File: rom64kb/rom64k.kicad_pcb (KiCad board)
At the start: 2 copper layers, 81.3 x 65.3 mm, 3 parts, among them P1 CONN_02X25, U2 SST39SF010

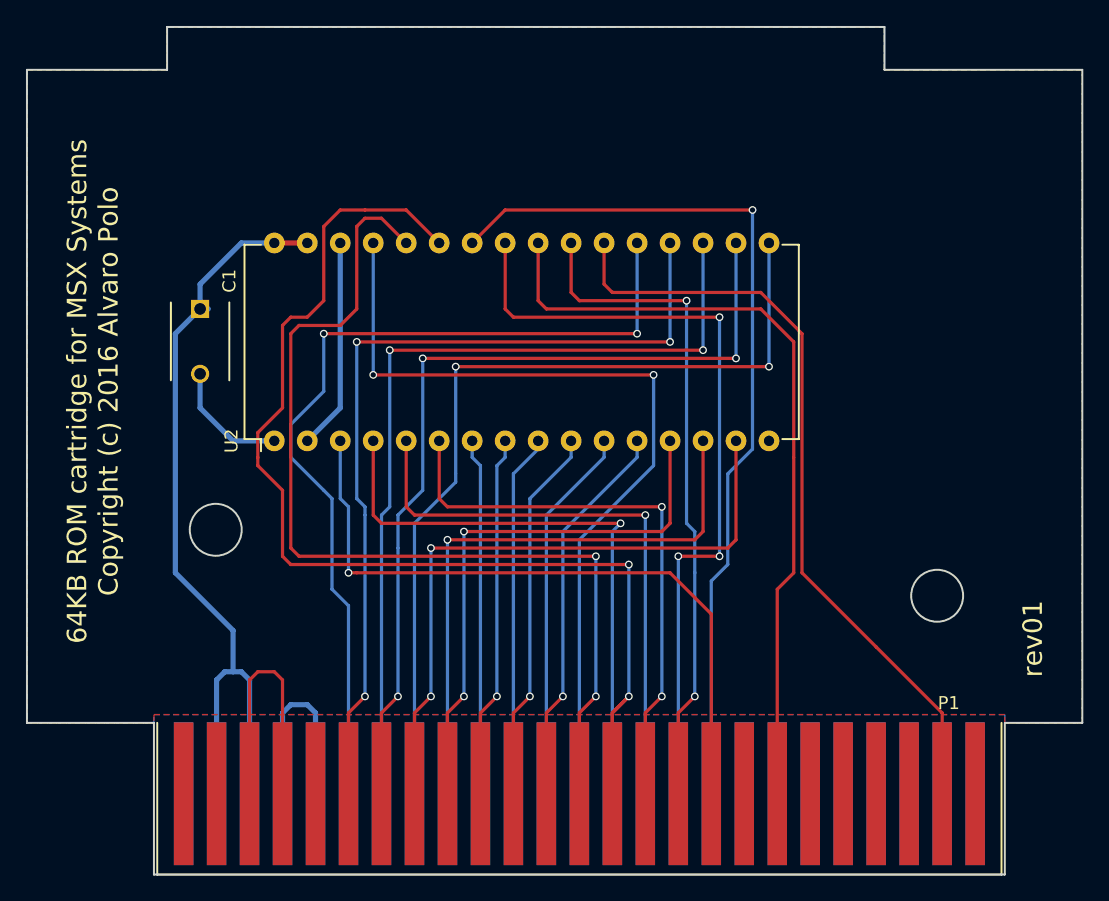
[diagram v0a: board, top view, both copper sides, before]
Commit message: Fixed hole placement, reduced PCB size for cost-cutting
Signed-off-by: filip <bolo-poczta@outlook.com>
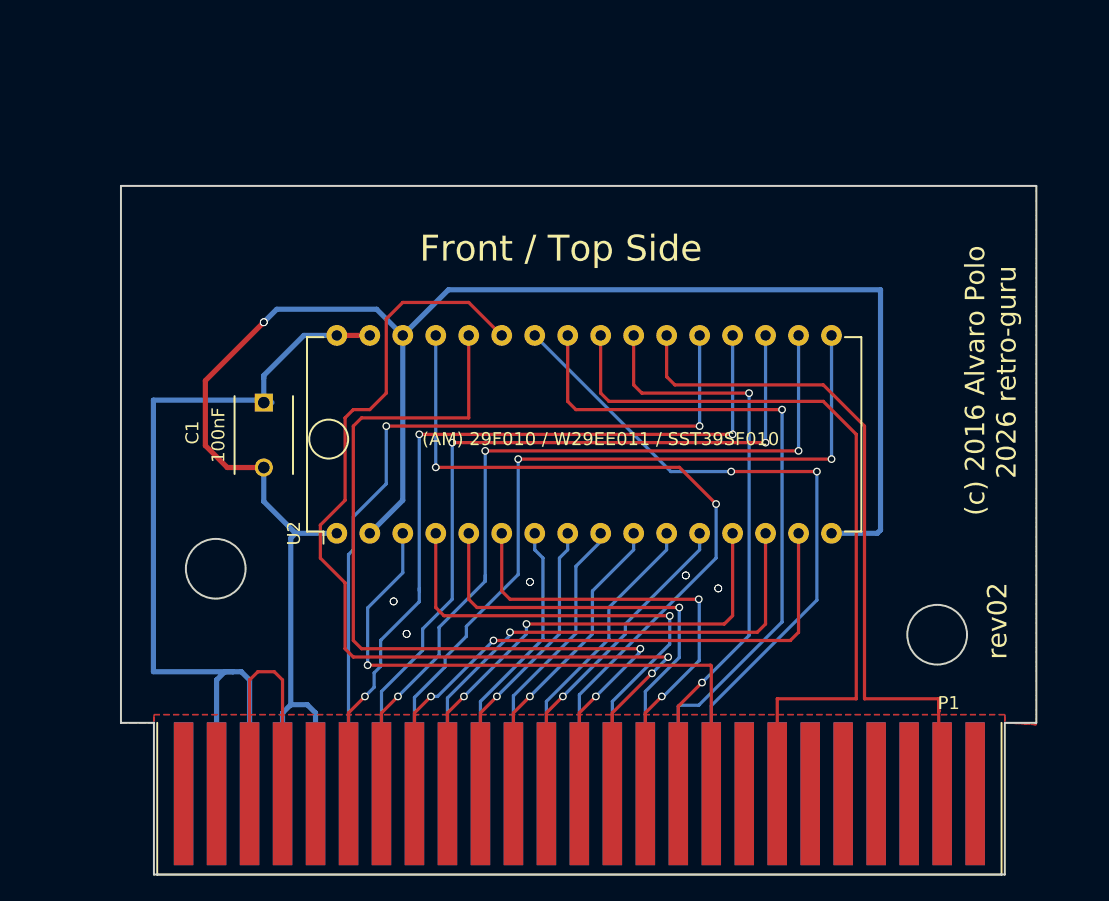
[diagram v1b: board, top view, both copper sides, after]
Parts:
- U2: value SST39SF010 -> (AM) 29F010 / W29EE011 / SST39SF010
- moved C1 8.72 mm to (130.0, 124.7)
- moved U2 8.60 mm to (135.6, 134.8)
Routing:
- net GND: track 41.2 -> 143.6 mm, vias 0 -> 12
- net /A9: track 68.9 -> 54.3 mm, vias 1 -> 2
- net /A8: track 92.6 -> 83.2 mm
- net ~{SLTSL}: track 59.9 -> 50.8 mm
- net /D7: track 69.4 -> 60.6 mm
- net /A13: track 76.2 -> 67.5 mm
- net /A7: track 45.2 -> 37.0 mm
- net /A6: track 44.5 -> 36.7 mm
- net /A14: track 66.4 -> 59.6 mm
- net /A12: track 46.1 -> 39.5 mm
- net /A11: track 61.7 -> 55.6 mm, vias 3 -> 1
- net /A15: track 53.5 -> 47.6 mm
- net /A10: track 51.7 -> 46.1 mm
- net /D6: track 67.3 -> 61.9 mm
- net /D5: track 66.8 -> 61.7 mm
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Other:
- board size 81.3 x 65.3 mm -> 70.5 x 53 mm
- board text added: "(c) 2016 Alvaro Polo 2026 retro-guru"
- board text added: "Front / Top Side"
- board text added: "rev02"
- board text removed: "64KB ROM cartridge for MSX Systems Copyright (c) 2016 Alvaro Polo"
- board text removed: "rev01"
